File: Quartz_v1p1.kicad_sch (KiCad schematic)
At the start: 5 parts, among them J1 5747847-6, J2 5747847-6

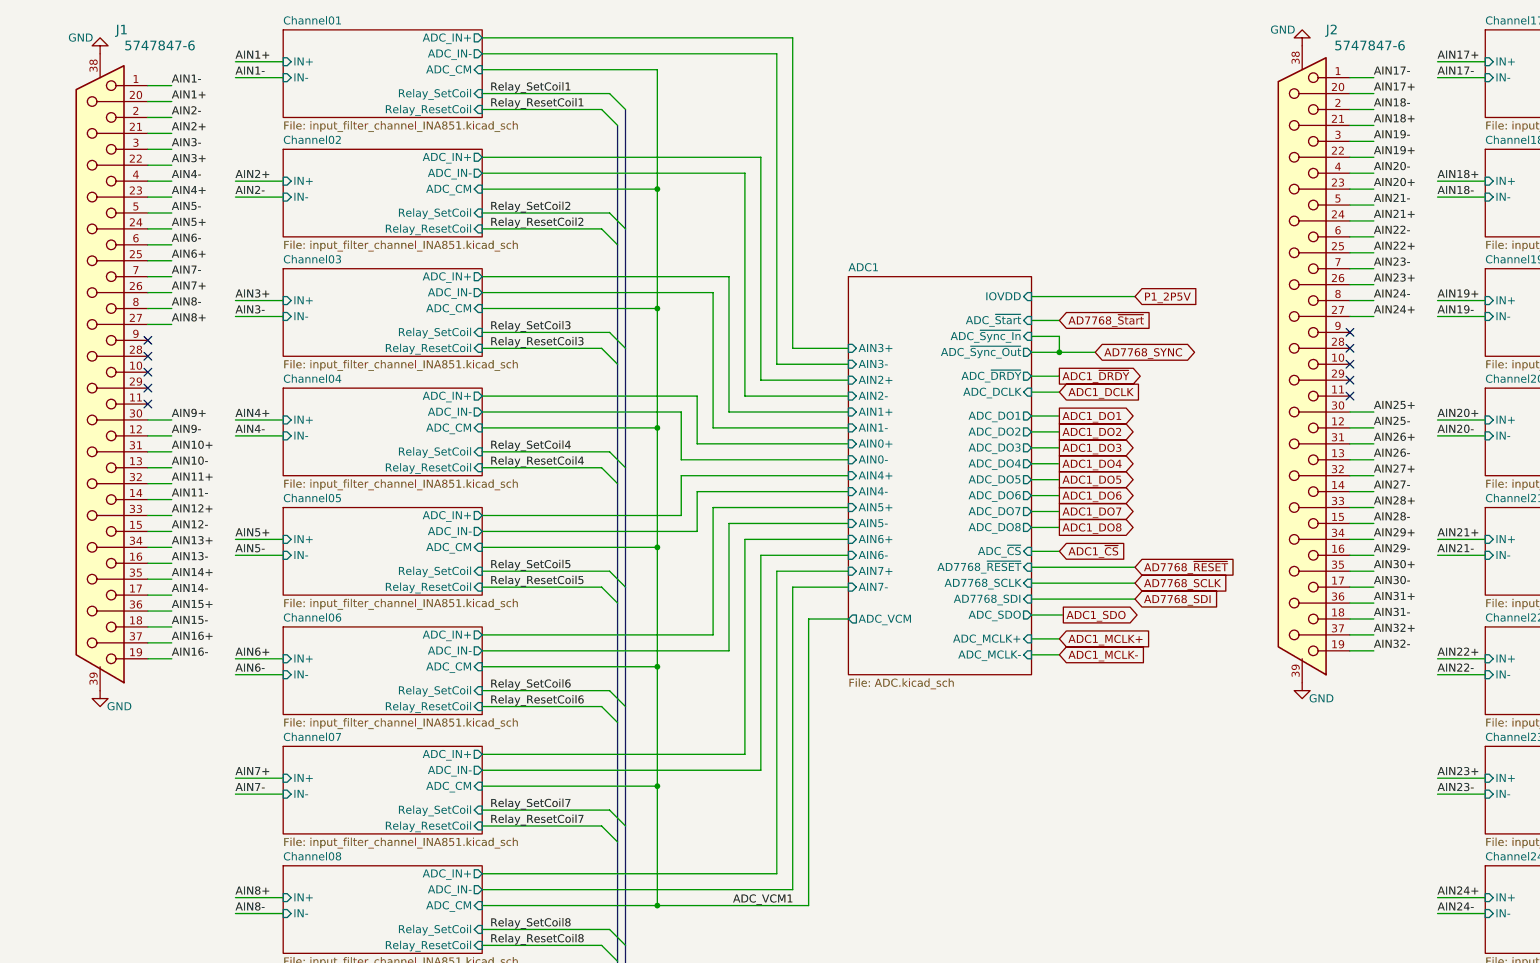
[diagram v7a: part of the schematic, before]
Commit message: Finalized Design & Board
Change to design
-Added resistor options to choose the grounding of input connectors
-uploaded libraries
-uploaded generated BOM
- adjusted mounting holes on front of board by 10mil
-Changed input AC blocking cap to 10nF from 100nF due to part availability
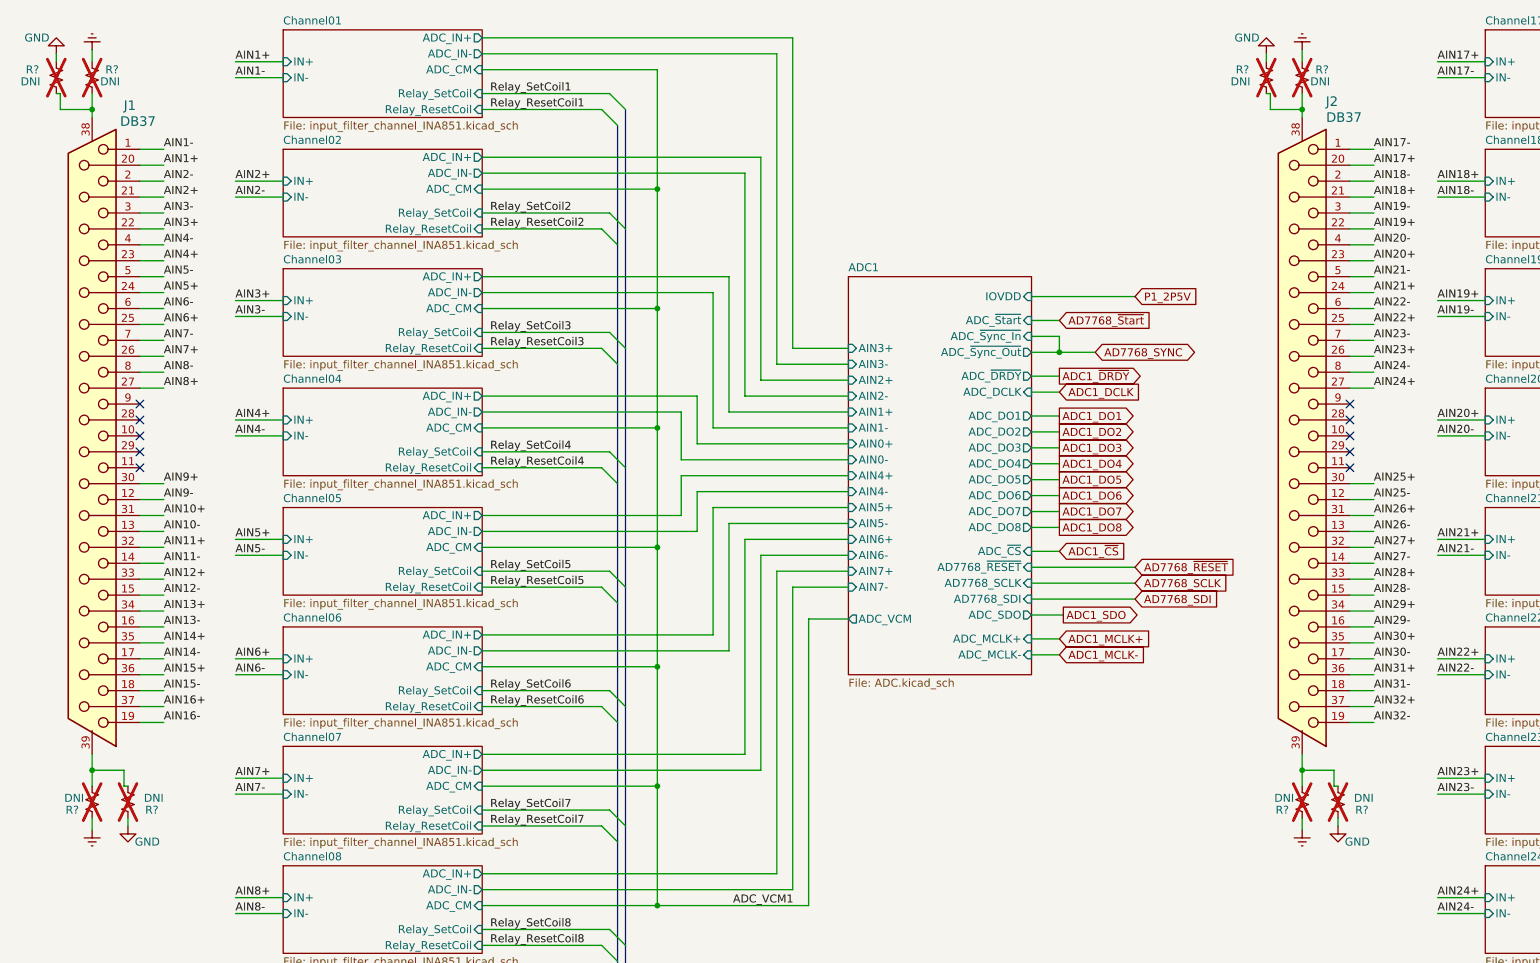
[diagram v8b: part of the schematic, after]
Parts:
- added R? (x8): DNI, Resistor_SMD:R_0805_2012Metric, symbol Device:R_Small_US
- J1, J2: value 5747847-6 -> DB37; footprint AD7768_Digitizer:CONN_5747847-6_TYC -> QuartzFootprints:CONN_5747847-6_TYC
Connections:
- net GND: now also R?.1, R?.1, R?.1, R?.1; no longer J1.38, J1.39, J2.38, J2.39
- new net: J1.39, R?.2, R?.2
- new net: J2.38, R?.2, R?.2
- new net: J1.38, R?.2, R?.2
- new net: J2.39, R?.2, R?.2
- new net Earth: R?.1, R?.1, R?.1, R?.1
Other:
- moved on the sheet: J1, J2
